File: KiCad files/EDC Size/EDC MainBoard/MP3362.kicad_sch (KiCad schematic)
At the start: 19 parts, among them J10 Conn_01x04, U1 MP3362GJ, U3 TPS61165DBV

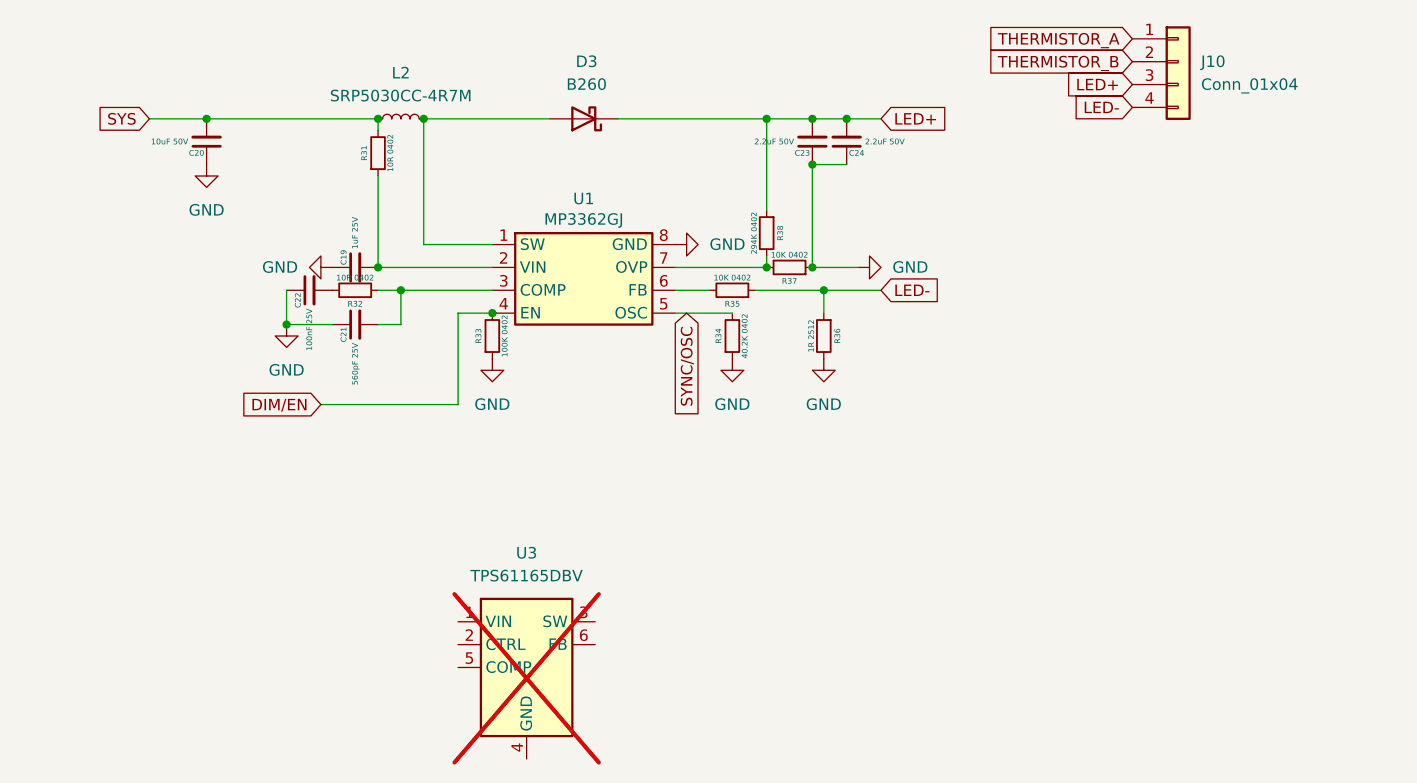
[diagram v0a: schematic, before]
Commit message: updated the schematics and completed the battery charge IC circuit
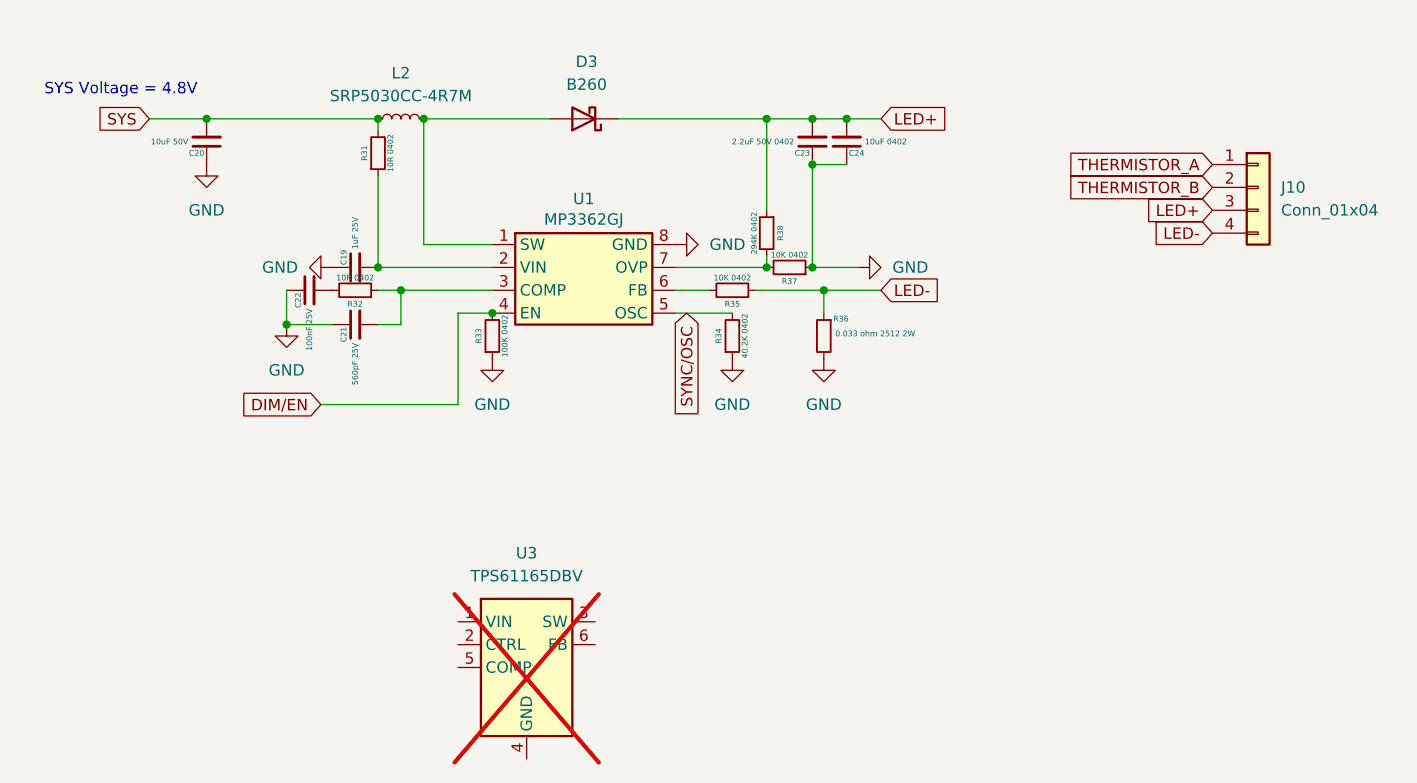
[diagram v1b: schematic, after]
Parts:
- C23: value 2.2uF 50V -> 2.2uF 50V 0402
- C24: value 2.2uF 50V -> 10uF 0402
- R36: value 1R 2512 -> 0.033 ohm 2512 2W
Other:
- note added: "SYS Voltage = 4.8V"
- moved on the sheet: J10
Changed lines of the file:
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@@
+		)
+	)
+	(text "SYS Voltage = 4.8V"
+		(exclude_from_sim no)
+		(at 26.035 32.385 0)
+		(effects
+			(font
+				(size 1.27 1.27)
+			)
 		)
 	)
@@
 	(global_label "LED+"
 		(shape input)
-		(at 138.43 31.75 180)
+		(at 147.32 45.72 180)
 		(fields_autoplaced yes)
 		(effects
@@
 		)
 		(property "Intersheetrefs" "${INTERSHEET_REFS}"
-			(at 130.4253 31.75 0)
+			(at 139.3153 45.72 0)
 			(effects
 				(font
@@
 	(global_label "THERMISTOR_A"
 		(shape input)
-		(at 138.43 26.67 180)
+		(at 147.32 40.64 180)
 		(fields_autoplaced yes)
 		(effects
@@
 		)
 		(property "Intersheetrefs" "${INTERSHEET_REFS}"
-			(at 121.8377 26.67 0)
+			(at 130.7277 40.64 0)
 			(effects
 				(font
@@
 	(global_label "THERMISTOR_B"
 		(shape input)
-		(at 138.43 29.21 180)
+		(at 147.32 43.18 180)
 		(fields_autoplaced yes)
 		(effects
@@
 		)
 		(property "Intersheetrefs" "${INTERSHEET_REFS}"
-			(at 121.6563 29.21 0)
+			(at 130.5463 43.18 0)
 			(effects
 				(font
@@
 	(global_label "LED-"
 		(shape input)
-		(at 138.43 34.29 180)
+		(at 147.32 48.26 180)
 		(fields_autoplaced yes)
 		(effects
@@
 		)
 		(property "Intersheetrefs" "${INTERSHEET_REFS}"
-			(at 130.4253 34.29 0)
+			(at 139.3153 48.26 0)
 			(effects
 				(font
@@
 	(symbol
 		(lib_id "Connector_Generic:Conn_01x04")
-		(at 143.51 29.21 0)
+		(at 152.4 43.18 0)
 		(unit 1)
 		(exclude_from_sim no)
@@
 		(fields_autoplaced yes)
 		(property "Reference" "J10"
-			(at 146.05 29.2099 0)
+			(at 154.94 43.1799 0)
 			(effects
 				(font
@@
 		)
 		(property "Value" "Conn_01x04"
-			(at 146.05 31.7499 0)
+			(at 154.94 45.7199 0)
 			(effects
 				(font
@@
 		)
 		(property "Footprint" "Connector_PinSocket_2.54mm:PinSocket_1x04_P2.54mm_Vertical"
-			(at 143.51 29.21 0)
+			(at 152.4 43.18 0)
 			(effects
 				(font
@@
 		)
 		(property "Datasheet" "~"
-			(at 143.51 29.21 0)
+			(at 152.4 43.18 0)
 			(effects
 				(font
@@
 		)
 		(property "Description" "Generic connector, single row, 01x04, script generated (kicad-library-utils/schlib/autogen/connector/)"
-			(at 143.51 29.21 0)
+			(at 152.4 43.18 0)
 			(effects
 				(font
@@
 		(dnp no)
 		(property "Reference" "R36"
-			(at 105.664 59.69 90)
-			(effects
-				(font
-					(size 0.635 0.635)
-				)
-			)
-		)
-		(property "Value" "1R 2512"
-			(at 103.124 59.69 90)
-			(effects
-				(font
-					(size 0.635 0.635)
-				)
-				(justify top)
+			(at 106.045 57.785 0)
+			(effects
+				(font
+					(size 0.635 0.635)
+				)
+			)
+		)
+		(property "Value" "0.033 ohm 2512 2W"
+			(at 105.41 59.055 0)
+			(effects
+				(font
+					(size 0.635 0.635)
+				)
+				(justify right top)
 			)
 		)
@@
 			)
 		)
-		(property "Value" "2.2uF 50V"
+		(property "Value" "10uF 0402"
 			(at 108.712 38.1 0)
 			(effects
@@
 			)
 		)
-		(property "Value" "2.2uF 50V"
+		(property "Value" "2.2uF 50V 0402"
 			(at 100.838 38.1 0)
 			(effects
